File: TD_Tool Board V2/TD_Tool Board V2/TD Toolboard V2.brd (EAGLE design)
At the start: 8.6 x 5 mm, 142 parts, among them J3 430450400CON_430450400_MOL, M1 NMOSFET_WSD3066DN33, M2 CJ3400, M3 CJ3400, M4 CJ3400, P1 TPS54202_BUCKCONV, P2 3.3V, U1 RP2040IC57_RP2040-L, U2 W25Q128JVSIQSOIC_128JVSIQ_WIN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, U3 SN65HVD1050DRD8-L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

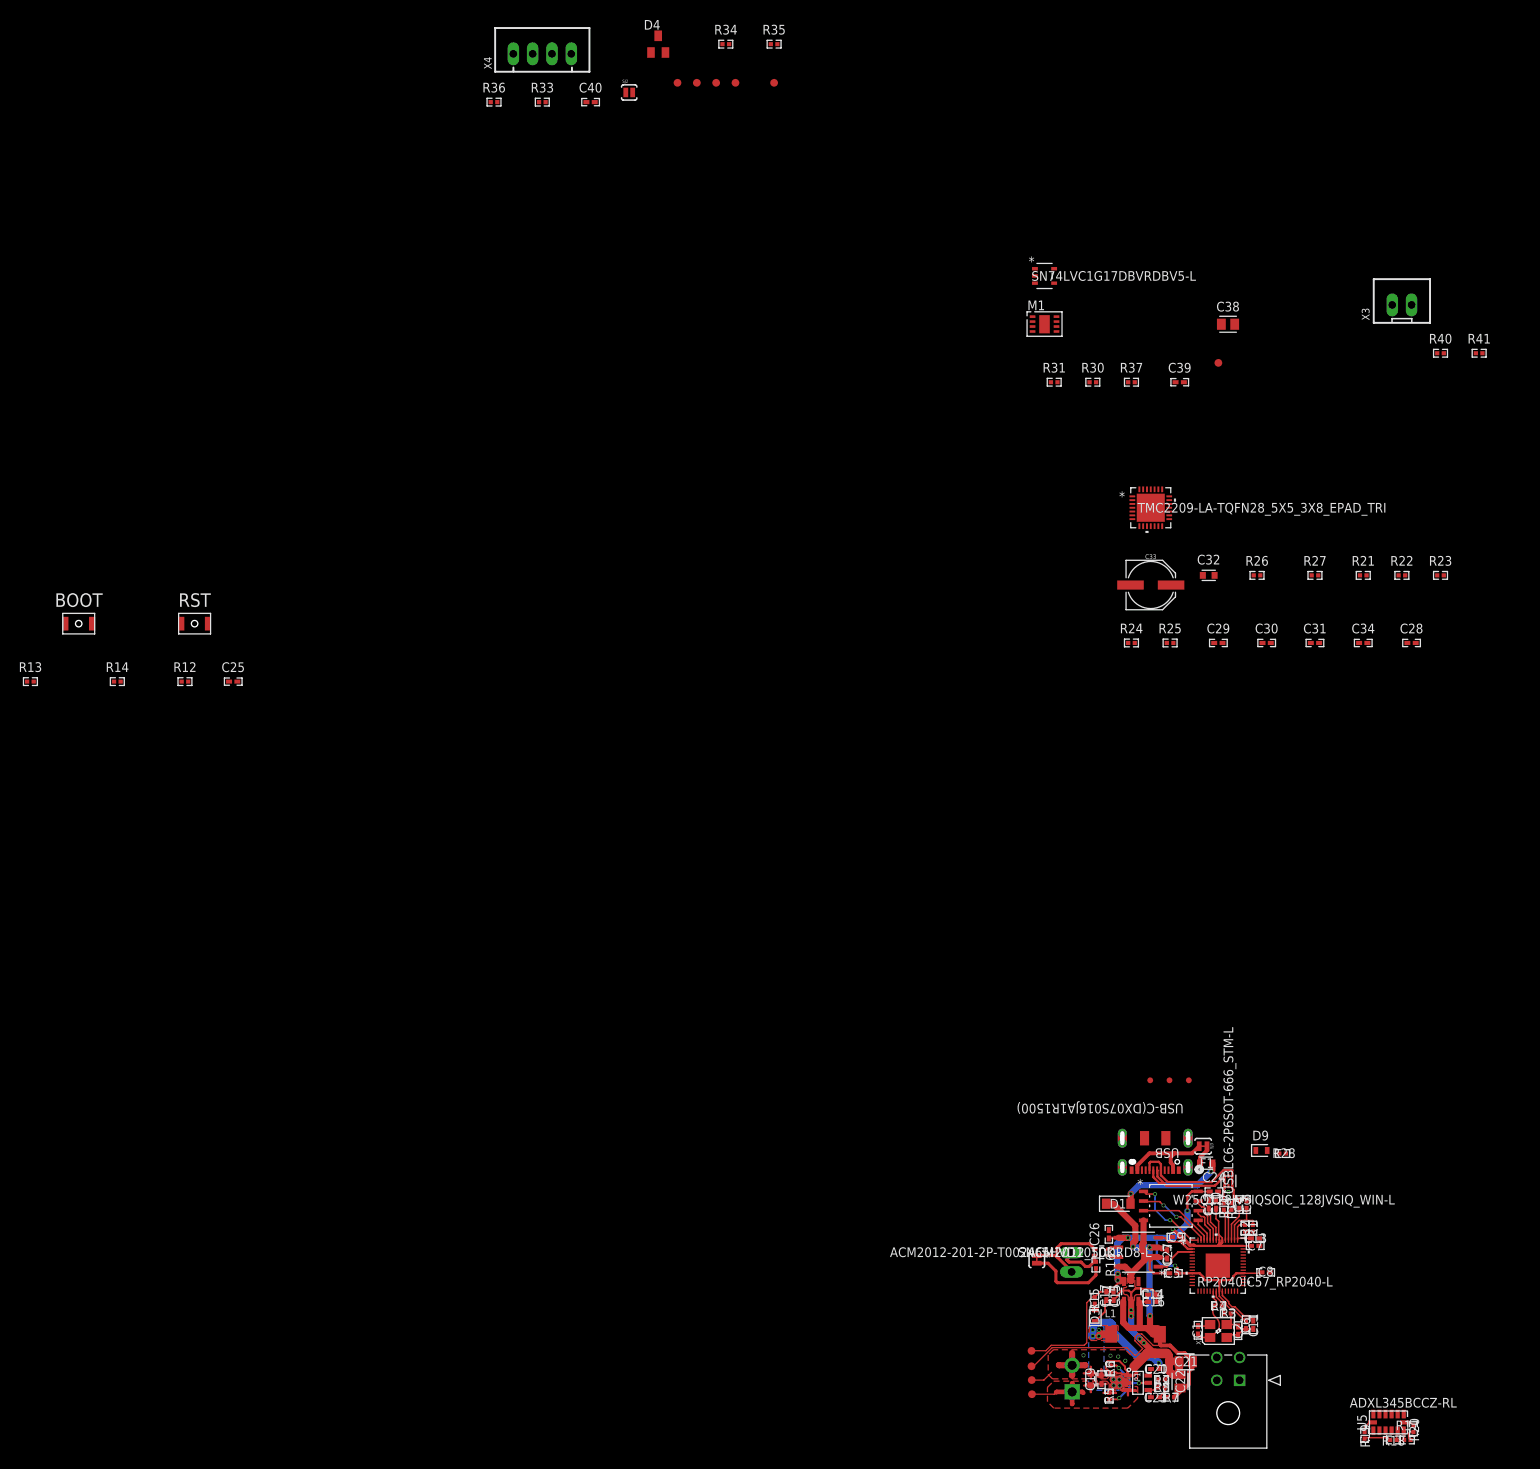
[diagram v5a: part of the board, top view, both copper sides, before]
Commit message: TMC routed
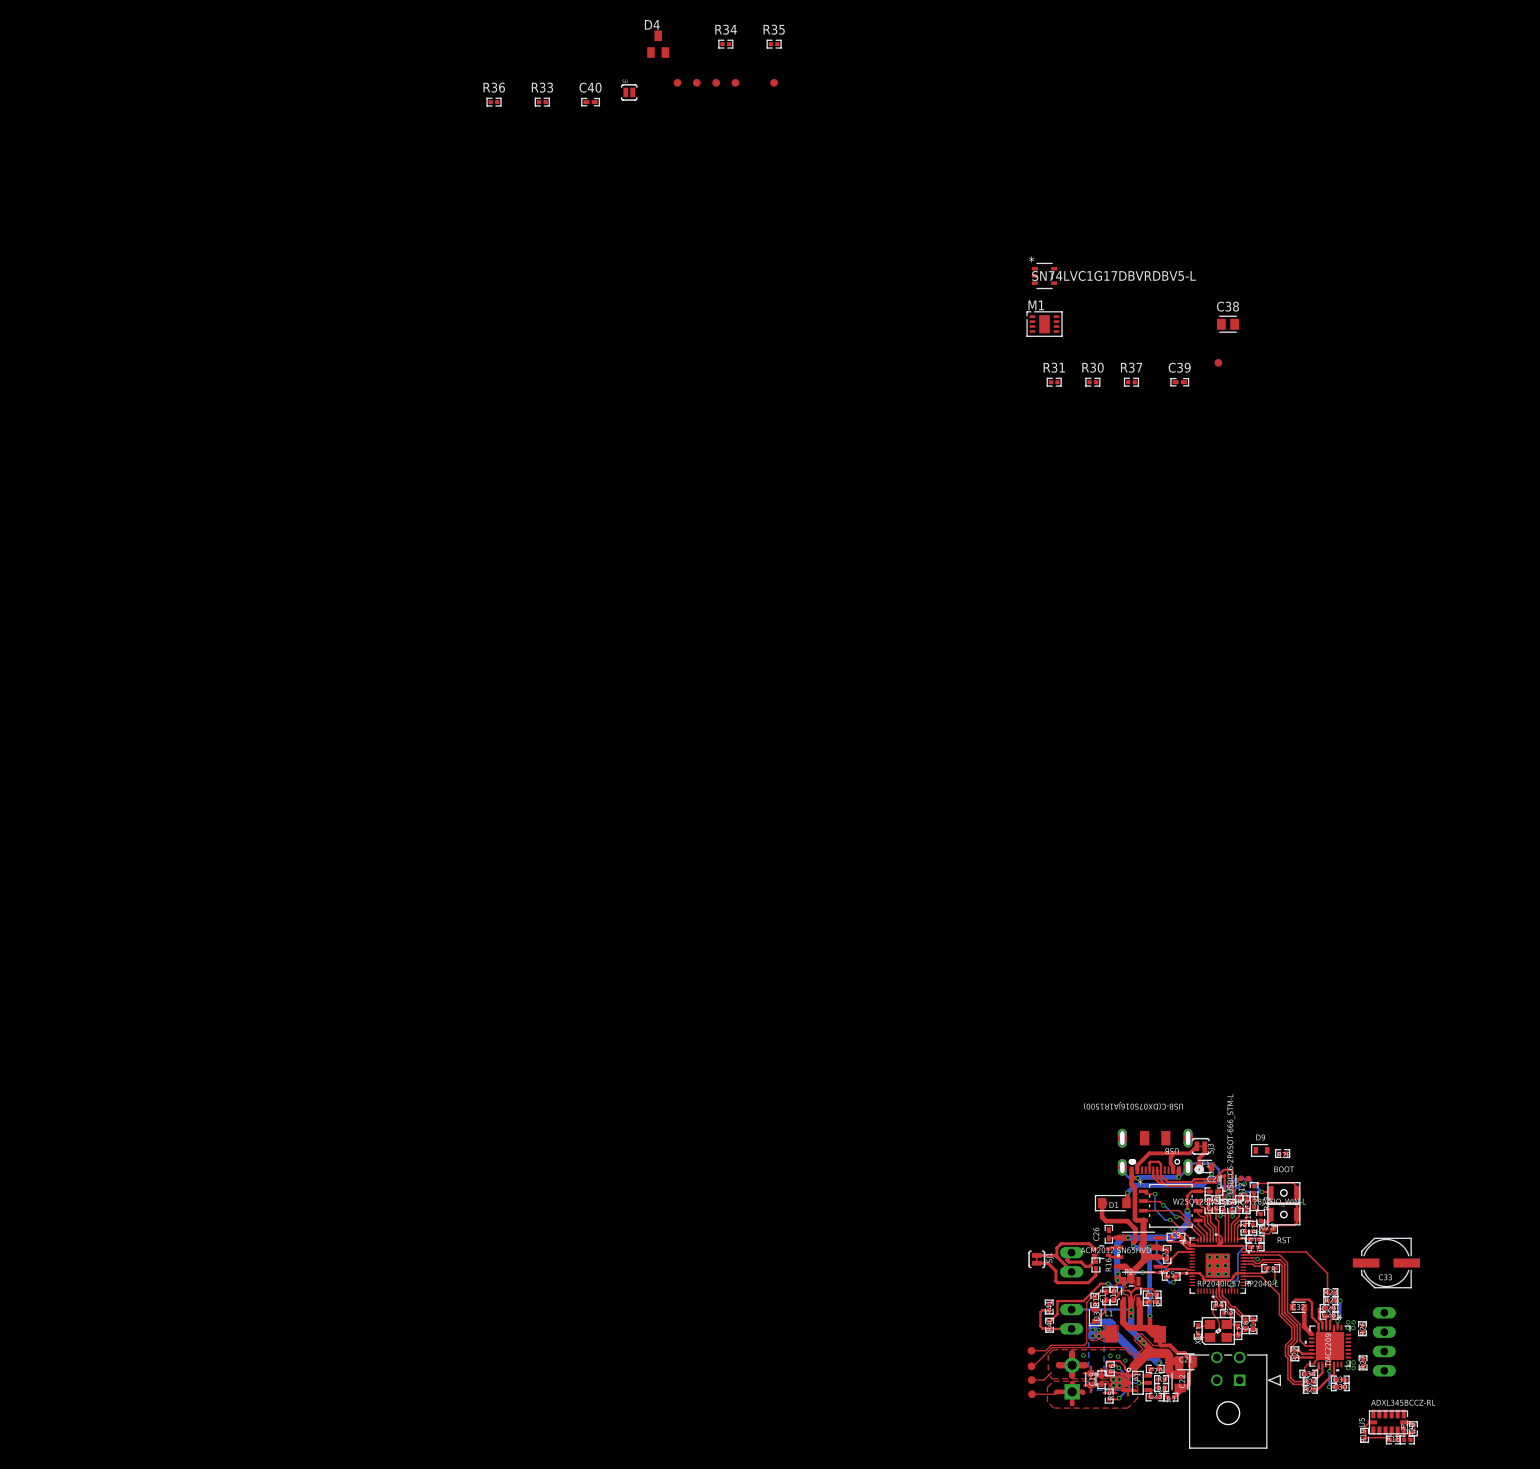
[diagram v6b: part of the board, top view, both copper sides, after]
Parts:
- removed IO3: TEST-POINT3, SparkFun-Connectors:PAD.03X.03
- removed X4: JST-XH-04-PIN-LONG-PAD, Rembrandt Electronics - JST XH Connectors v1-0:JST-XH-04-PACKAGE-LONG-PAD
- added EXTRUDER: JST-XH-04-PIN-LONG-PAD, Rembrandt Electronics - JST XH Connectors v1-0:JST-XH-04-PACKAGE-LONG-PAD
- L2: value ACM2012-201-2P-T002ACM2012_TDK -> ACM2012
- U3: value SN65HVD1050DRD8-L -> SN65HVD
- U7: value TMC2209-LA-TQFN28_5X5_3X8_EPAD_TRI -> TMC2209
- moved BOOT 175.3 mm to (125.5, -17.7)
- moved R13 174.9 mm to (121.5, -19.1), turned to 270 degrees
- moved R14 166.0 mm to (122.4, -20.9), turned to 90 degrees
- moved RST 162.9 mm to (125.5, -20.5), turned to 180 degrees
- moved R12 155.7 mm to (121.5, -17.3), turned to 90 degrees
- moved C25 154.0 mm to (123.4, -22.5), turned to 180 degrees
- moved X3 140.3 mm to (97.5, -34.3), flipped to the bottom, turned to 270 degrees
- moved R40 137.8 mm to (94.6, -35.1), turned to 270 degrees
- moved R41 137.6 mm to (94.6, -32.7), turned to 270 degrees
- moved U7 112.7 mm to (131.5, -37.8), turned to 270 degrees
- moved R27 103.7 mm to (135.9, -40.1), turned to 90 degrees
- moved R22 103.3 mm to (126.9, -38.9), turned to 270 degrees
- moved R26 100.0 mm to (135.8, -35.6), turned to 270 degrees
- moved R24 99.9 mm to (128.9, -42.5)
- moved R25 99.9 mm to (128.9, -43.5)
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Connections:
- net +5V: no longer IO3.P$1
- net A1: now also EXTRUDER.2; no longer X4.2
- net A2: now also EXTRUDER.1; no longer X4.1
- net B1: now also EXTRUDER.3; no longer X4.3
- net B2: now also EXTRUDER.4; no longer X4.4
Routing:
- net GND: track 90.8 -> 178.0 mm, vias 8 -> 27
- net E0_STEP: track 0.00 -> 23.9 mm
- net ENDSTOP_X: track 0.00 -> 23.0 mm, vias 0 -> 2
- net E0_UART: track 0.00 -> 21.7 mm
- net E0_DIR: track 0.00 -> 21.1 mm
- net E0_DIAG: track 0.00 -> 19.0 mm
- net E0_EN: track 0.00 -> 14.8 mm
- net RESET: track 0.00 -> 14.7 mm, vias 0 -> 2
- net EX: track 0.00 -> 7.33 mm
- net USB_P: track 4.09 -> 11.3 mm, vias 0 -> 2
- net USB_N: track 4.24 -> 11.4 mm, vias 0 -> 2
- net SWB: track 0.00 -> 6.82 mm
- net +3.3V: track 107.6 -> 113.3 mm
- net TMCENN: track 0.00 -> 5.58 mm, vias 0 -> 2
- net DIR: track 0.00 -> 4.89 mm
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- added copper zone on layer 16, net GND
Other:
- board text removed: "Accelerometer"
- board text removed: "BUCK"
- board text removed: "Buttons"
- board text removed: "CAN"
- board text removed: "Crystal"
- board text removed: "FLASH"
- board text removed: "LDO"
- board text removed: "MCU"

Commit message: Minor Changes
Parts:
- moved R26 1.00 mm to (135.7, -34.6)
- moved C28 0.55 mm to (131.3, -33.3)
- moved C29 0.55 mm to (131.3, -32.3)
- moved C34 0.55 mm to (128.6, -41.0)
- moved R21 0.55 mm to (131.5, -31.3)
- moved C32 0.55 mm to (127.3, -32.2)
- moved R22 0.55 mm to (126.8, -38.3)
- moved R23 0.55 mm to (131.5, -30.3)
- moved R24 0.55 mm to (128.8, -42.0)
- moved R25 0.55 mm to (128.8, -43.0)
- moved U7 0.55 mm to (131.4, -37.3)
- moved C31 0.51 mm to (132.9, -42.8)
- moved C30 0.51 mm to (132.9, -43.7)
- moved R27 0.31 mm to (135.7, -39.8)
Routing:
- net +24V: track 19.0 -> 46.0 mm, vias 8 -> 11
- net GND: track 178.0 -> 196.0 mm, vias 27 -> 46
- net B1: track 0.00 -> 10.3 mm
- net A1: track 0.00 -> 10.3 mm
- net B2: track 0.00 -> 9.93 mm
- net A2: track 0.00 -> 9.90 mm
- net BRB: track 0.00 -> 2.43 mm
- net BRA: track 0.00 -> 2.35 mm
- net E0_DIAG: track 19.0 -> 18.4 mm
- net E0_STEP: track 23.9 -> 23.3 mm
- net E0_UART: track 21.7 -> 21.1 mm
- net E0_EN: track 14.8 -> 14.2 mm
- added copper zone on layer 16, net +24V
- added copper zone on layer 1, net A1
- added copper zone on layer 1, net A2
- added copper zone on layer 1, net B1
- added copper zone on layer 1, net B2

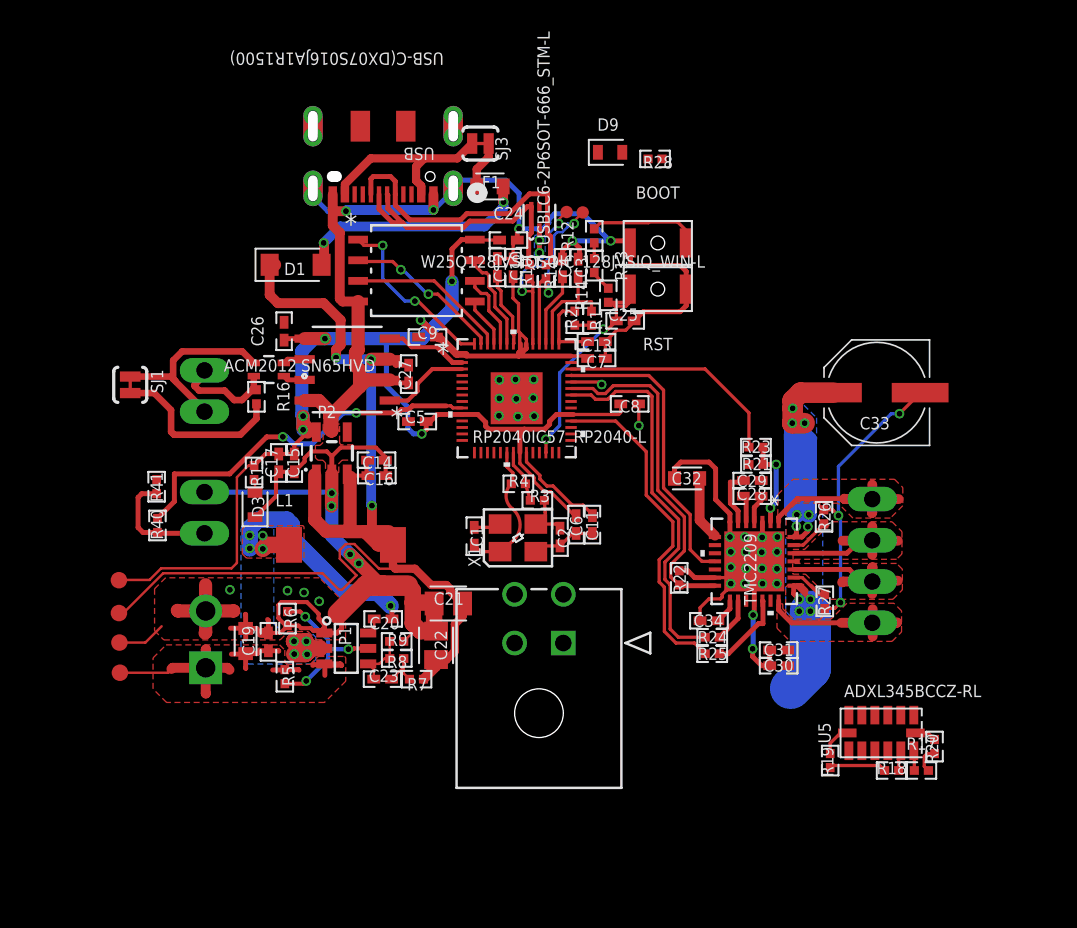
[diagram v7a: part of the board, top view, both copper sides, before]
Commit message: Added holes, made board dimension layout, few other minor changes
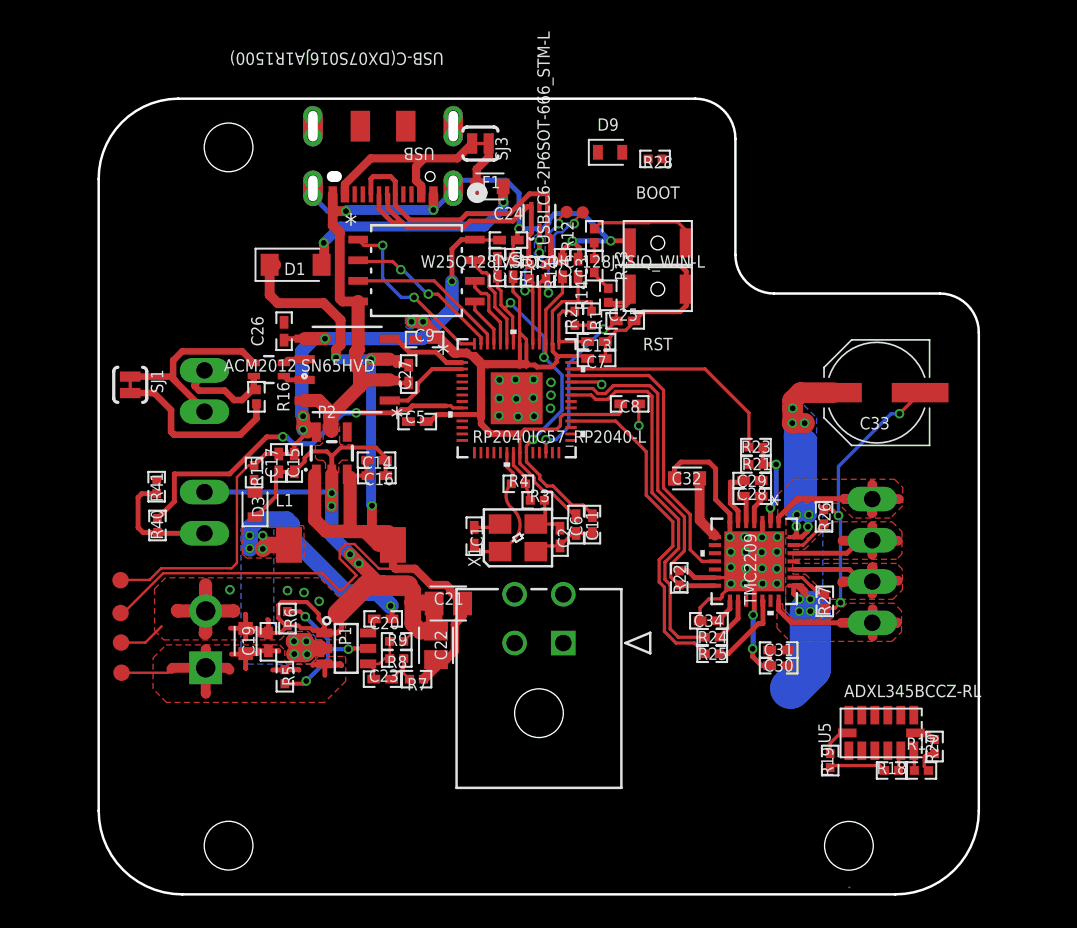
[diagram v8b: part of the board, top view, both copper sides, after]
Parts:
- moved C9 0.23 mm to (111.1, -23.7)
- moved 24V 0.10 mm to (92.4, -44.2)
- moved 3.3V 0.10 mm to (92.4, -38.5)
- moved 5V 0.10 mm to (92.4, -40.5)
- moved GND 0.10 mm to (92.4, -42.3)
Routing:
- net +1.1V: track 15.3 -> 28.2 mm, vias 0 -> 3
- net +3.3V: track 113.3 -> 116.9 mm
- net GND: track 196.0 -> 195.9 mm, vias 46 -> 49
- added copper zone on layer 16, net +3.3V
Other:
- board size 8.6 x 5 mm -> 54.2 x 49 mm
